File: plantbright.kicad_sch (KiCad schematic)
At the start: 0 parts

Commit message: Add temp MOSFET
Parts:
- added Q1, Q2: AO3400A, Package_TO_SOT_SMD:SOT-23, symbol Transistor_FET:AO3400A
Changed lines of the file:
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@@
 	(generator_version "9.0")
 	(paper "A4")
+	(symbol
+		(lib_id "Transistor_FET:AO3400A")
+		(at 110.49 101.6 0)
+		(unit 1)
+		(exclude_from_sim no)
+		(in_bom yes)
+		(on_board yes)
+		(dnp no)
+		(fields_autoplaced yes)
+		(property "Reference" "Q1"
+			(at 116.84 100.3299 0)
+			(effects
+				(font
+					(size 1.27 1.27)
+				)
+				(justify left)
+			)
+		)
+		(property "Value" "AO3400A"
+			(at 116.84 102.8699 0)
+			(effects
+				(font
+					(size 1.27 1.27)
+				)
+				(justify left)
+			)
+		)
+		(property "Footprint" "Package_TO_SOT_SMD:SOT-23"
+			(at 115.57 103.505 0)
+			(effects
+				(font
+					(size 1.27 1.27)
+					(italic yes)
+				)
+				(justify left)
+				(hide yes)
+			)
+		)
+		(property "Datasheet" "http://www.aosmd.com/pdfs/datasheet/AO3400A.pdf"
+			(at 115.57 105.41 0)
+			(effects
+				(font
+					(size 1.27 1.27)
+				)
+				(justify left)
+				(hide yes)
+			)
+		)
+		(property "Description" "30V Vds, 5.7A Id, N-Channel MOSFET, SOT-23"
+			(at 110.49 101.6 0)
+			(effects
+				(font
+					(size 1.27 1.27)
+				)
+				(hide yes)
+			)
+		)
+		(pin "3"
+		)
+		(pin "2"
+		)
+		(pin "1"
+		)
+		(instances
+			(project ""
+				(path "/e2caaa62-12a4-4d86-8d92-9420077836ea"
+					(reference "Q1")
+					(unit 1)
+				)
+			)
+		)
+	)
+	(symbol
+		(lib_id "Transistor_FET:AO3400A")
+		(at 110.49 115.57 0)
+		(unit 1)
+		(exclude_from_sim no)
+		(in_bom yes)
+		(on_board yes)
+		(dnp no)
+		(fields_autoplaced yes)
+		(property "Reference" "Q2"
+			(at 116.84 114.2999 0)
+			(effects
+				(font
+					(size 1.27 1.27)
+				)
+				(justify left)
+			)
+		)
+		(property "Value" "AO3400A"
+			(at 116.84 116.8399 0)
+			(effects
+				(font
+					(size 1.27 1.27)
+				)
+				(justify left)
+			)
+		)
+		(property "Footprint" "Package_TO_SOT_SMD:SOT-23"
+			(at 115.57 117.475 0)
+			(effects
+				(font
+					(size 1.27 1.27)
+					(italic yes)
+				)
+				(justify left)
+				(hide yes)
+			)
+		)
+		(property "Datasheet" "http://www.aosmd.com/pdfs/datasheet/AO3400A.pdf"
+			(at 115.57 119.38 0)
+			(effects
+				(font
+					(size 1.27 1.27)
+				)
+				(justify left)
+				(hide yes)
+			)
+		)
+		(property "Description" "30V Vds, 5.7A Id, N-Channel MOSFET, SOT-23"
+			(at 110.49 115.57 0)
+			(effects
+				(font
+					(size 1.27 1.27)
+				)
+				(hide yes)
+			)
+		)
+		(pin "3"
+		)
+		(pin "2"
+		)
+		(pin "1"
+		)
+		(instances
+			(project "plantbright"
+				(path "/e2caaa62-12a4-4d86-8d92-9420077836ea"
+					(reference "Q2")
+					(unit 1)
+				)
+			)
+		)
+	)
 	(sheet_instances
 		(path "/"

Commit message: Wow, wow. Why a DF Player Mini?
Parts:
- added J1: POWER OUT, symbol Connector:Screw_Terminal_01x06
- added J2: SPEAKER, symbol Connector:Screw_Terminal_01x02
- added Q3, Q4, Q5: AO3400A, Package_TO_SOT_SMD:SOT-23-3, symbol Transistor_FET:AO3400A
- added R1, R11, R4, R7, R8: 100R, symbol Device:R
- added R2, R3, R5, R6, R9: 10K, symbol Device:R
- added U1: XIAO-ESP32-C6, Seeed Studio XIAO Series Library:XIAO-ESP32C6-DIP, symbol Seeed_Studio_XIAO_Series:XIAO_ESP32-C6-DIP
- Q1, Q2: footprint Package_TO_SOT_SMD:SOT-23 -> Package_TO_SOT_SMD:SOT-23-3
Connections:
- net at Q1.1 (G): now also R1.2
- net GND: now reaches Q1.2 (S)
- net GND: now also Q2.2 (S), Q3.2 (S), Q4.2 (S), Q5.2 (S), R2.2, R3.2, R5.2, R6.2, R9.2, U1.13 (GND)
- net SW_1: now reaches Q1.3 (D)
- net SW_1: now also J1.2 (Pin_2)
- net at Q2.1 (G): now also R4.2
- net SW_2: now reaches Q2.3 (D)
- net SW_2: now also J1.3 (Pin_3)
- new net: Q4.1 (G), R8.2
- new net: Q3.1 (G), R7.2
- new net: Q5.1 (G), R11.2
- new net +5V: J1.1 (Pin_1), U1.14 (VBUS)
- new net CH_1: R1.1, R2.1
- new net CH_2: R3.1, R4.1
- new net CH_3: R5.1, R7.1
- new net CH_4: R6.1, R8.1
- new net CH_5: R11.1, R9.1
- new net DF_L: J2.1 (Pin_1)
- new net DF_R: J2.2 (Pin_2)
- new net DF_RX: U1.7 (GPIO16/D6/TX)
- new net DF_TX: U1.8 (GPIO17/D7/RX)
- new net SW_3: J1.4 (Pin_4), Q3.3 (D)
- new net SW_4: J1.5 (Pin_5), Q4.3 (D)
- new net SW_5: J1.6 (Pin_6), Q5.3 (D)
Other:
- note added: "I/O"
- note added: "MOSFETs"

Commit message: Start board layout
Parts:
- added J3: USB_C_Receptacle_USB2.0_14P, Connector_USB:USB_C_Receptacle_HRO_TYPE-C-31-M-12, symbol Connector:USB_C_Receptacle_USB2.0_14P
- added R11, R12: 10K, Resistor_SMD:R_0805_2012Metric_Pad1.20x1.40mm_HandSolder, symbol Device:R
- added R13, R14: 5.1K, Resistor_SMD:R_0805_2012Metric_Pad1.20x1.40mm_HandSolder, symbol Device:R
- added SW1, SW2: SW_Push, Button_Switch_THT:SW_PUSH_6mm, symbol Switch:SW_Push
- R1, R2: footprint (none) -> Resistor_SMD:R_0805_2012Metric_Pad1.20x1.40mm_HandSolder
- R10: renamed from R9; footprint (none) -> Resistor_SMD:R_0805_2012Metric_Pad1.20x1.40mm_HandSolder
- R3: renamed from R4; footprint (none) -> Resistor_SMD:R_0805_2012Metric_Pad1.20x1.40mm_HandSolder
- R4: renamed from R3; footprint (none) -> Resistor_SMD:R_0805_2012Metric_Pad1.20x1.40mm_HandSolder
- R5: renamed from R7; footprint (none) -> Resistor_SMD:R_0805_2012Metric_Pad1.20x1.40mm_HandSolder
- R6: renamed from R5; footprint (none) -> Resistor_SMD:R_0805_2012Metric_Pad1.20x1.40mm_HandSolder
- R7: renamed from R8; footprint (none) -> Resistor_SMD:R_0805_2012Metric_Pad1.20x1.40mm_HandSolder
- R8: renamed from R6; footprint (none) -> Resistor_SMD:R_0805_2012Metric_Pad1.20x1.40mm_HandSolder
- R9: renamed from R11; footprint (none) -> Resistor_SMD:R_0805_2012Metric_Pad1.20x1.40mm_HandSolder
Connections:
- net +5V: now also J3.A4 (VBUS), J3.A9 (VBUS), J3.B4 (VBUS), J3.B9 (VBUS)
- net CH_1: now also U1.1 (GPIO0/A0/D0)
- net CH_2: now also U1.2 (GPIO1/A1/D1)
- net CH_3: now also U1.3 (GPIO2/A2/D2), U1.4 (GPIO21/D3)
- net CH_4: now also U1.11 (GPIO18/D10/MOSI)
- net CH_5: now also U1.10 (GPIO20/D9/MISO)
- net GND: now also J3.A1 (GND), J3.A12 (GND), J3.B1 (GND), J3.B12 (GND), J3.S1 (SHIELD), R11.2, R12.2, R13.2, R14.2
- net +3.3V: now reaches U1.12 (3V3)
- net +3.3V: now also SW1.2, SW2.2
- net BTN_1: now reaches U1.5 (GPIO22/D4/SDA)
- net BTN_1: now also R11.1, SW1.1
- net BTN_2: now reaches U1.6 (GPIO23/D5/SCL)
- net BTN_2: now also R12.1, SW2.1
- net BUSY: now reaches U1.9 (GPIO19/D8/SCK)
- new net: J3.B5 (CC2), R13.1
- new net: J3.A5 (CC1), R14.1
- no-connect marks 0 -> 4
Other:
- note added: "BUTTONS"
- note added: "OUTPUT"
- note added: "POWER"
- note removed: "I/O"
- moved on the sheet: J1, J2, Q1, Q2, Q3, Q4, Q5, R1, R10, R2, R3, R4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

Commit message: Enough for now. Arranging bits.
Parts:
- J1: footprint (none) -> Connector_JST:JST_XH_B6B-XH-A_1x06_P2.50mm_Vertical
- J2: footprint (none) -> Connector_JST:JST_XH_B2B-XH-A_1x02_P2.50mm_Vertical
- SW1: value SW_Push -> USER 0
- SW2: value SW_Push -> USER 1
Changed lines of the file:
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@@
 			)
 		)
-		(property "Footprint" ""
+		(property "Footprint" "Connector_JST:JST_XH_B6B-XH-A_1x06_P2.50mm_Vertical"
 			(at 39.37 118.11 0)
 			(effects
@@
 			)
 		)
-		(property "Value" "SW_Push"
+		(property "Value" "USER 1"
 			(at 97.79 114.2999 90)
 			(effects
@@
 			)
 		)
-		(property "Footprint" ""
+		(property "Footprint" "Connector_JST:JST_XH_B2B-XH-A_1x02_P2.50mm_Vertical"
 			(at 39.37 130.81 0)
 			(effects
@@
 			)
 		)
-		(property "Value" "SW_Push"
+		(property "Value" "USER 0"
 			(at 74.93 114.2999 90)
 			(effects

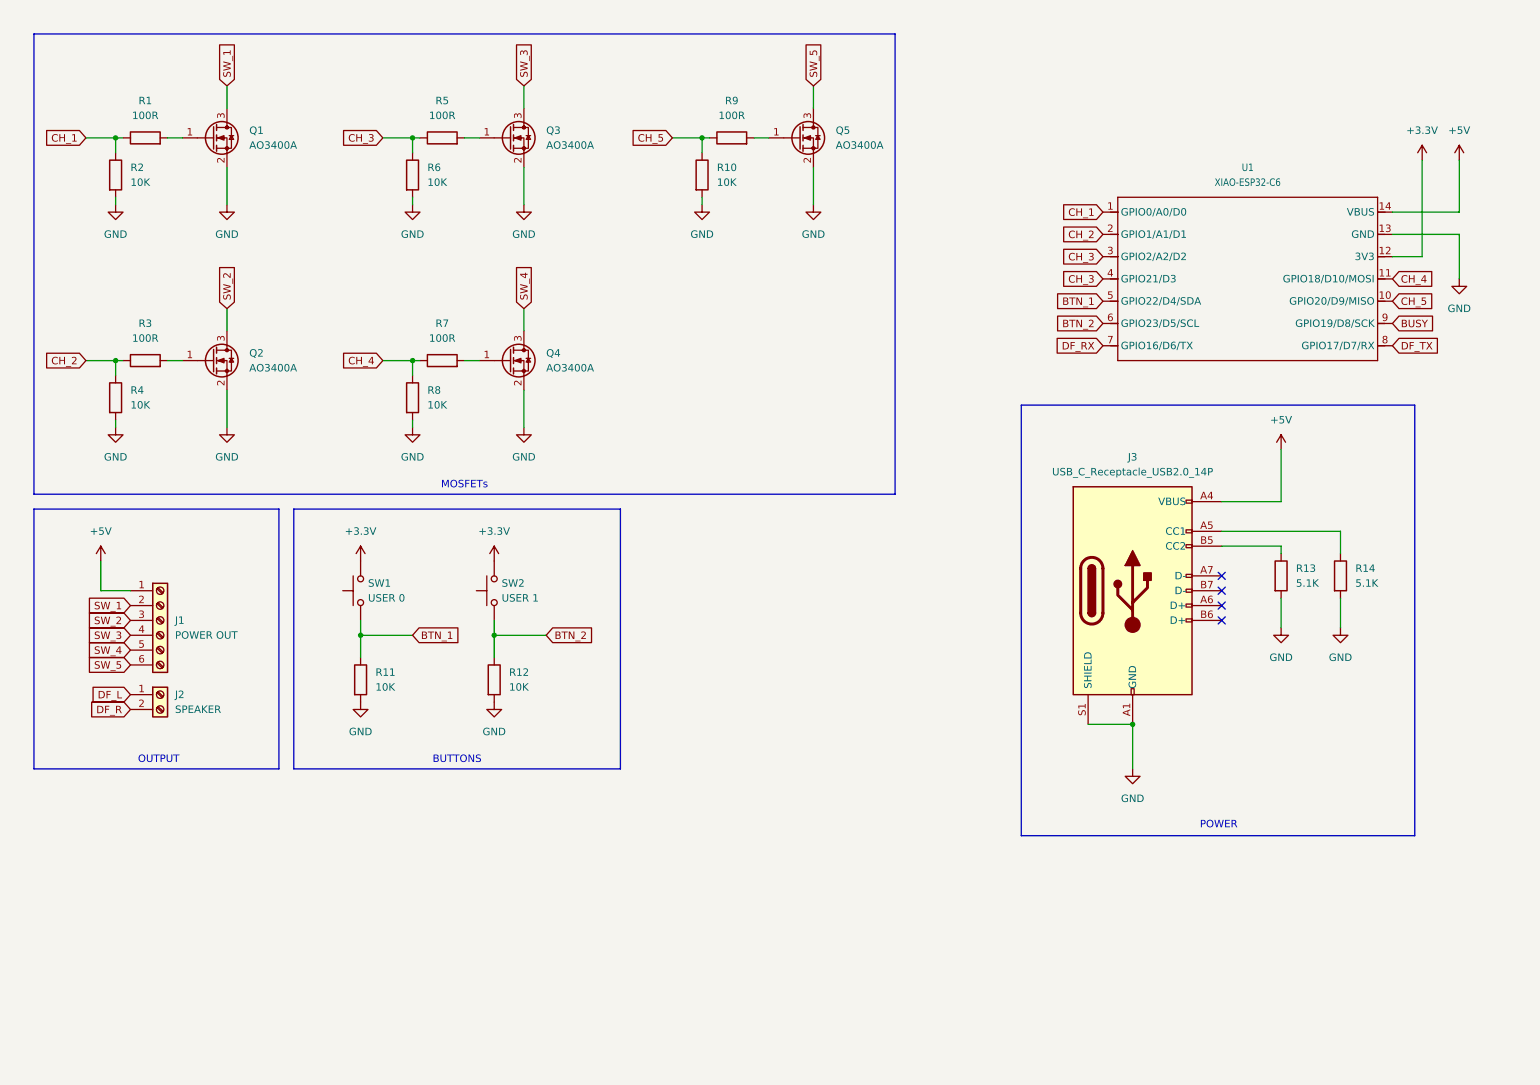
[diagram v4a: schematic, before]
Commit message: Add in dfplayermini board.
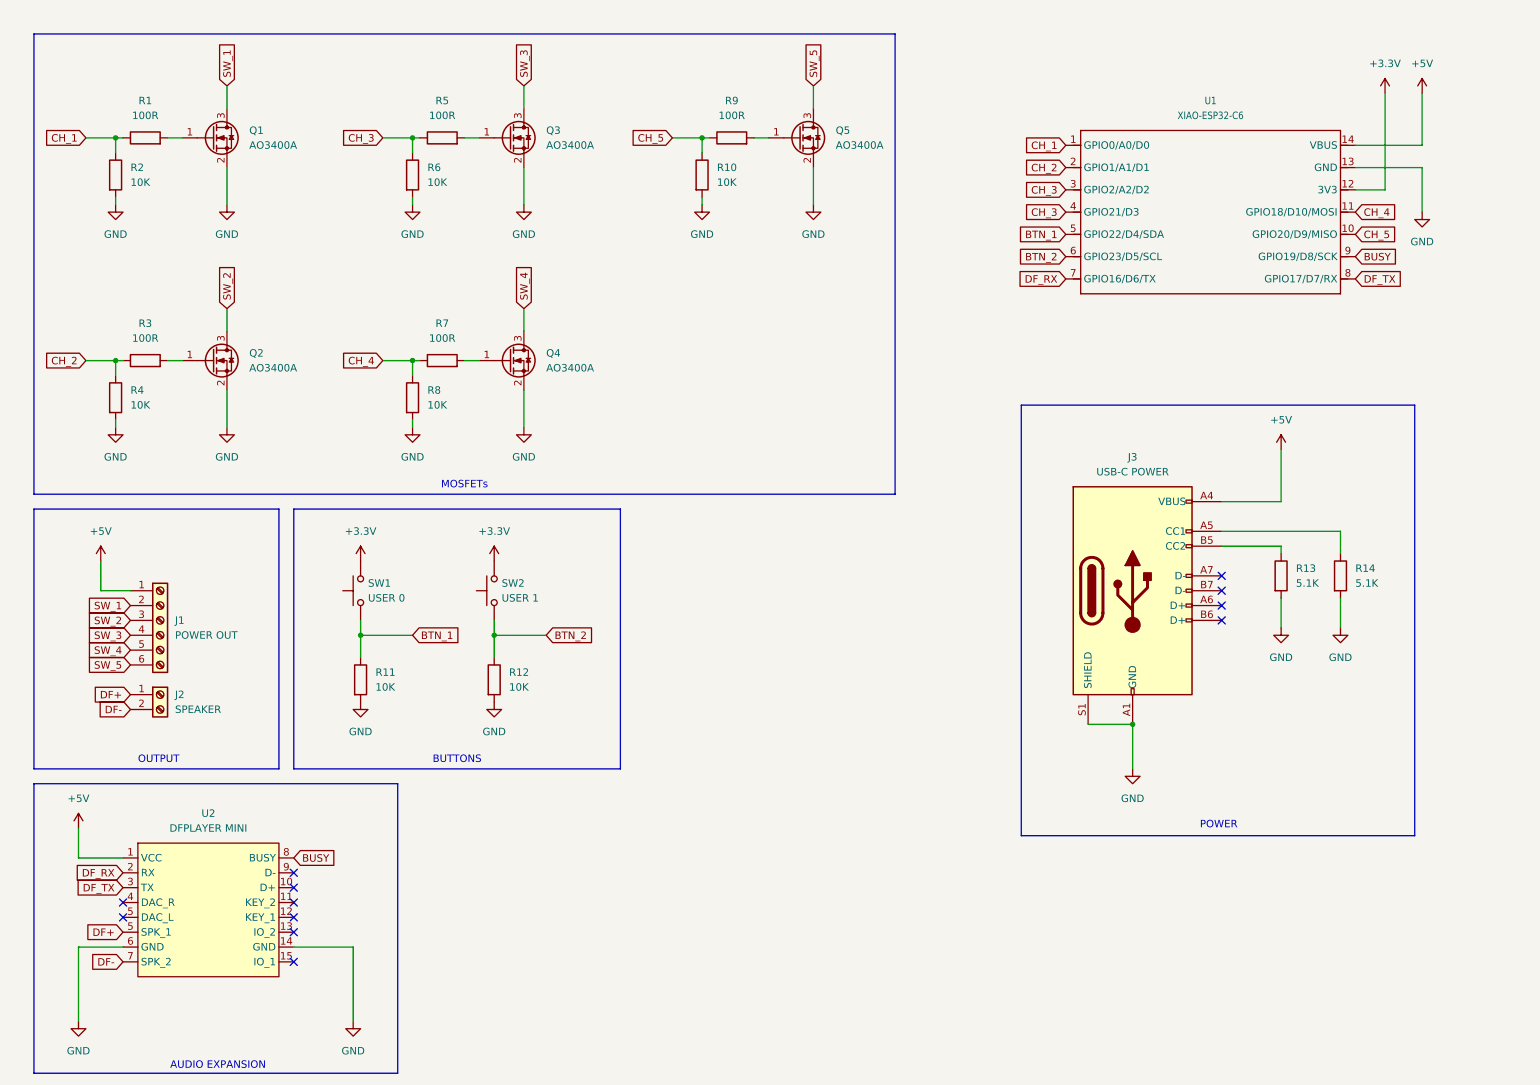
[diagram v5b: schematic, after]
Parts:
- added U2: DFPLAYER MINI, kicad-dfplayermini:dfplayer, symbol dfplayer:DFPlayerMini
- J3: value USB_C_Receptacle_USB2.0_14P -> USB-C POWER
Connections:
- net +5V: now also U2.1 (VCC)
- net BUSY: now also U2.8 (BUSY)
- net DF_RX: now also U2.2 (RX)
- net DF_TX: now also U2.3 (TX)
- net GND: now also U2.14 (GND), U2.6 (GND)
- net DF_L renamed DF+
- net DF+: now also U2.5 (SPK_1)
- net DF_R renamed DF-
- net DF-: now also U2.7 (SPK_2)
- no-connect marks 4 -> 12
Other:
- note added: "AUDIO EXPANSION"
- moved on the sheet: U1

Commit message: Update `dfmini` library
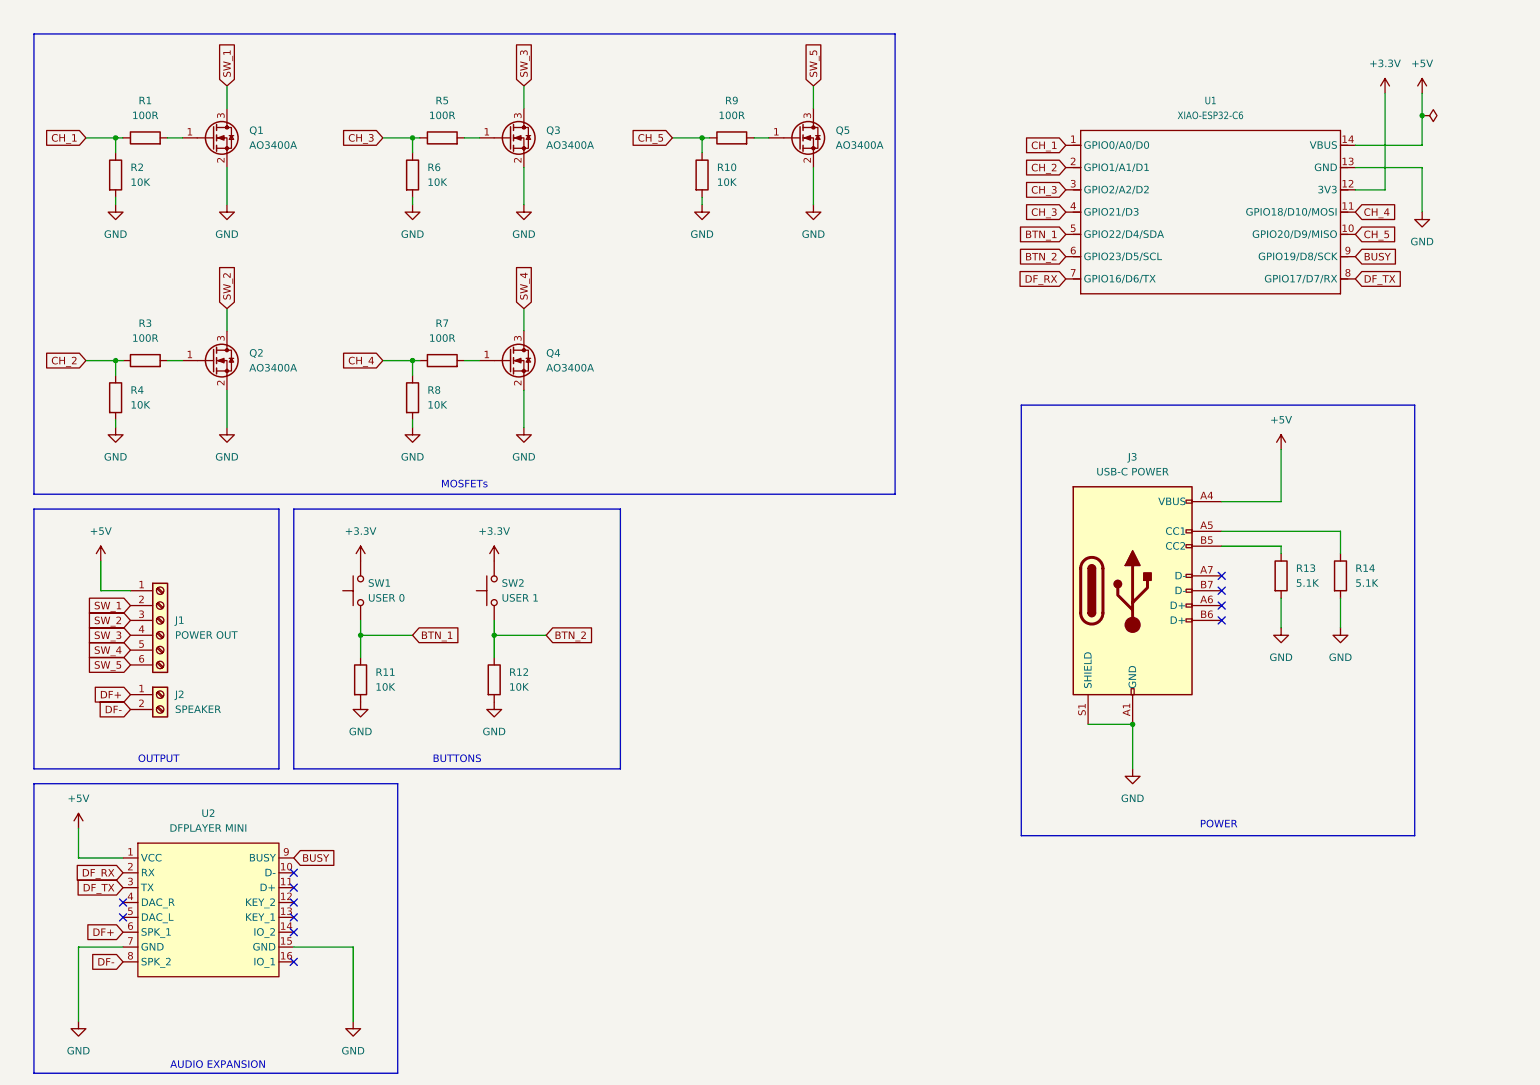
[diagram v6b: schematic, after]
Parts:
- Q1, Q2, Q3, Q4, Q5: footprint Package_TO_SOT_SMD:SOT-23-3 -> Package_TO_SOT_SMD:SOT-23
- U1: footprint Seeed Studio XIAO Series Library:XIAO-ESP32C6-DIP -> Module:MOUDLE14P-XIAO-DIP-SMD
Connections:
- net BUSY: now also U2.9 (BUSY); no longer U2.8 (BUSY)
- net DF+: now also U2.6 (SPK_1); no longer U2.5 (SPK_1)
- net DF-: now also U2.8 (SPK_2); no longer U2.7 (SPK_2)
- net GND: now also U2.15 (GND), U2.7 (GND); no longer U2.14 (GND), U2.6 (GND)
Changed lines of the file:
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@@
 	)
 	(junction
+		(at 255.27 31.75)
+		(diameter 0)
+		(color 0 0 0 0)
+	)
+	(junction
 		(at 31.75 73.66)
 		(diameter 0)
@@
 	(wire
 		(pts
+			(xy 255.27 31.75) (xy 255.27 27.94)
+		)
+		(stroke
+			(width 0)
+			(type default)
+		)
+	)
+	(wire
+		(pts
 			(xy 82.55 45.72) (xy 82.55 46.99)
 		)
@@
 	(wire
 		(pts
-			(xy 255.27 36.83) (xy 255.27 27.94)
+			(xy 255.27 36.83) (xy 255.27 31.75)
 		)
 		(stroke
@@
 	(wire
 		(pts
-			(xy 25.4 158.75) (xy 25.4 153.67)
+			(xy 25.4 153.67) (xy 25.4 158.75)
 		)
 		(stroke
@@
 			)
 		)
-		(property "Footprint" "Package_TO_SOT_SMD:SOT-23-3"
+		(property "Footprint" "Package_TO_SOT_SMD:SOT-23"
 			(at 104.14 75.565 0)
 			(effects
@@
 			)
 		)
-		(property "Footprint" "Package_TO_SOT_SMD:SOT-23-3"
+		(property "Footprint" "Package_TO_SOT_SMD:SOT-23"
 			(at 104.14 37.465 0)
 			(effects
@@
 			)
 		)
-		(property "Footprint" "Package_TO_SOT_SMD:SOT-23-3"
+		(property "Footprint" "Package_TO_SOT_SMD:SOT-23"
 			(at 53.34 75.565 0)
 			(effects
@@
 	)
 	(symbol
+		(lib_id "power:PWR_FLAG")
+		(at 255.27 31.75 270)
+		(unit 1)
+		(exclude_from_sim no)
+		(in_bom yes)
+		(on_board yes)
+		(dnp no)
+		(fields_autoplaced yes)
+		(property "Reference" "#FLG01"
+			(at 257.175 31.75 0)
+			(effects
+				(font
+					(size 1.27 1.27)
+				)
+				(hide yes)
+			)
+		)
+		(property "Value" "PWR_FLAG"
+			(at 259.08 31.7499 90)
+			(effects
+				(font
+					(size 1.27 1.27)
+				)
+				(justify left)
+				(hide yes)
+			)
+		)
+		(property "Footprint" ""
+			(at 255.27 31.75 0)
+			(effects
+				(font
+					(size 1.27 1.27)
+				)
+				(hide yes)
+			)
+		)
+		(property "Datasheet" "~"
+			(at 255.27 31.75 0)
+			(effects
+				(font
+					(size 1.27 1.27)
+				)
+				(hide yes)
+			)
+		)
+		(property "Description" "Special symbol for telling ERC where power comes from"
+			(at 255.27 31.75 0)
+			(effects
+				(font
+					(size 1.27 1.27)
+				)
+				(hide yes)
+			)
+		)
+		(pin "1"
+		)
+		(instances
+			(project ""
+				(path "/e2caaa62-12a4-4d86-8d92-9420077836ea"
+					(reference "#FLG01")
+					(unit 1)
+				)
+			)
+		)
+	)
+	(symbol
 		(lib_id "power:+3.3V")
 		(at 248.92 27.94 0)
@@
 			)
 		)
-		(property "Footprint" "Seeed Studio XIAO Series Library:XIAO-ESP32C6-DIP"
+		(property "Footprint" "Module:MOUDLE14P-XIAO-DIP-SMD"
 			(at 213.868 66.802 0)
 			(effects
@@
 		(pin "5"
 		)
-		(pin "5"
+		(pin "16"
 		)
 		(pin "4"
@@
 			)
 		)
-		(property "Footprint" "Package_TO_SOT_SMD:SOT-23-3"
+		(property "Footprint" "Package_TO_SOT_SMD:SOT-23"
 			(at 53.34 37.465 0)
 			(effects
@@
 			)
 		)
-		(property "Footprint" "Package_TO_SOT_SMD:SOT-23-3"
+		(property "Footprint" "Package_TO_SOT_SMD:SOT-23"
 			(at 153.67 37.465 0)
 			(effects

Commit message: Start layout again
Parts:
- removed J3: USB-C POWER, Connector_USB:USB_C_Receptacle_HRO_TYPE-C-31-M-12, symbol Connector:USB_C_Receptacle_USB2.0_14P
- removed R13, R14: 5.1K, Resistor_SMD:R_0805_2012Metric_Pad1.20x1.40mm_HandSolder, symbol Device:R
- added J4: 5V IN, Connector_JST:JST_XH_B2B-XH-A_1x02_P2.50mm_Vertical, symbol Connector:Screw_Terminal_01x02
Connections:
- net +5V: now also J4.1 (Pin_1)
- net GND: now also J4.2 (Pin_2)
- no-connect marks 12 -> 8
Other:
- note removed: "POWER"
